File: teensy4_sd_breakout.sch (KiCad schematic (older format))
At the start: 3 parts, among them J1 Conn_01x09, J2 Micro_SD_Card_Det

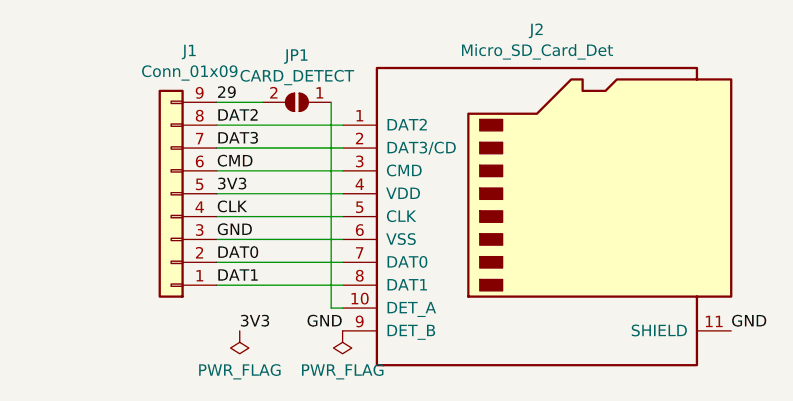
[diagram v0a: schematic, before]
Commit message: Added decoupling cap and back silk screen
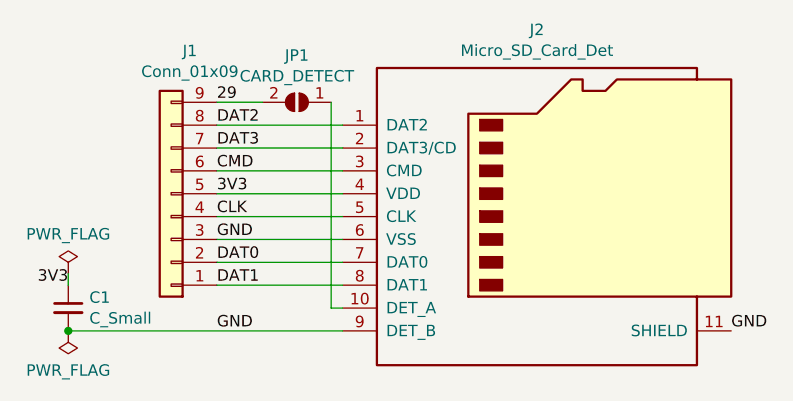
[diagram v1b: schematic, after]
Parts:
- added C1: C_Small, Capacitor_SMD:C_0805_2012Metric_Pad1.15x1.40mm_HandSolder, symbol Device:C_Small
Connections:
- net 3V3: now also C1.1
- net GND: now also C1.2
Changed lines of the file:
@@
 EESchema Schematic File Version 4
+LIBS:teensy4_sd_breakout-cache
 EELAYER 30 0
 EELAYER END
@@
 Text Label 6500 2450 0    50   ~ 0
 DAT2
-$Comp
-L Connector:Micro_SD_Card_Det J2
-U 1 1 5D85967D
-P 7950 2850
-F 0 "J2" H 7900 3667 50  0000 C CNN
-F 1 "Micro_SD_Card_Det" H 7900 3576 50  0000 C CNN
-F 2 "Connector_Card:microSD_HC_Hirose_DM3D-SF" H 10000 3550 50  0001 C CNN
-F 3 "https://www.hirose.com/product/en/download_file/key_name/DM3/category/Catalog/doc_file_id/49662/?file_category_id=4&item_id=195&is_series=1" H 7950 2950 50  0001 C CNN
-	1    7950 2850
-	1    0    0    -1
-$EndComp
 Text Label 8750 3350 0    50   ~ 0
 GND
-Text Label 7050 3350 2    50   ~ 0
+Text Label 6500 3350 0    50   ~ 0
 GND
-Wire Wire Line
-	7050 2450 6500 2450
-Wire Wire Line
-	7050 2550 6500 2550
-Wire Wire Line
-	6500 2650 7050 2650
-Wire Wire Line
-	7050 2750 6500 2750
-Wire Wire Line
-	6500 2850 7050 2850
-Wire Wire Line
-	7050 2950 6500 2950
-Wire Wire Line
-	6500 3050 7050 3050
-Wire Wire Line
-	7050 3150 6500 3150
 $Comp
 L Connector_Generic:Conn_01x09 J1
@@
 Wire Wire Line
 	7000 2350 7000 3250
-Wire Wire Line
-	7000 3250 7050 3250
 Text Label 6500 2350 0    50   ~ 0
 29
 $Comp
+L power:PWR_FLAG #FLG0102
+U 1 1 5D867552
+P 5850 3100
+F 0 "#FLG0102" H 5850 3175 50  0001 C CNN
+F 1 "PWR_FLAG" H 5850 3273 50  0000 C CNN
+F 2 "" H 5850 3100 50  0001 C CNN
+F 3 "~" H 5850 3100 50  0001 C CNN
+	1    5850 3100
+	1    0    0    -1
+$EndComp
+$Comp
+L Device:C_Small C1
+U 1 1 5D8A3C4C
+P 5850 3250
+F 0 "C1" H 5942 3296 50  0000 L CNN
+F 1 "C_Small" H 5942 3205 50  0000 L CNN
+F 2 "Capacitor_SMD:C_0805_2012Metric_Pad1.15x1.40mm_HandSolder" H 5850 3250 50  0001 C CNN
+F 3 "~" H 5850 3250 50  0001 C CNN
+	1    5850 3250
+	1    0    0    -1
+$EndComp
+Text Label 5850 3150 2    50   ~ 0
+3V3
+Wire Wire Line
+	7050 3150 6500 3150
+Wire Wire Line
+	6500 3050 7050 3050
+Wire Wire Line
+	7050 2950 6500 2950
+Wire Wire Line
+	6500 2850 7050 2850
+Wire Wire Line
+	7050 2750 6500 2750
+Wire Wire Line
+	6500 2650 7050 2650
+Wire Wire Line
+	7050 2550 6500 2550
+Wire Wire Line
+	7000 3250 7050 3250
+Wire Wire Line
+	7050 2450 6500 2450
+$Comp
+L Connector:Micro_SD_Card_Det J2
+U 1 1 5D85967D
+P 7950 2850
+F 0 "J2" H 7900 3667 50  0000 C CNN
+F 1 "Micro_SD_Card_Det" H 7900 3576 50  0000 C CNN
+F 2 "Connector_Card:microSD_HC_Hirose_DM3D-SF" H 10000 3550 50  0001 C CNN
+F 3 "https://www.hirose.com/product/en/download_file/key_name/DM3/category/Catalog/doc_file_id/49662/?file_category_id=4&item_id=195&is_series=1" H 7950 2950 50  0001 C CNN
+	1    7950 2850
+	1    0    0    -1
+$EndComp
+$Comp
 L power:PWR_FLAG #FLG0101
 U 1 1 5D86631A
-P 7050 3350
-F 0 "#FLG0101" H 7050 3425 50  0001 C CNN
-F 1 "PWR_FLAG" H 7050 3523 50  0000 C CNN
-F 2 "" H 7050 3350 50  0001 C CNN
-F 3 "~" H 7050 3350 50  0001 C CNN
-	1    7050 3350
+P 5850 3350
+F 0 "#FLG0101" H 5850 3425 50  0001 C CNN
+F 1 "PWR_FLAG" H 5850 3523 50  0000 C CNN
+F 2 "" H 5850 3350 50  0001 C CNN
+F 3 "~" H 5850 3350 50  0001 C CNN
+	1    5850 3350
 	-1   0    0    1
 $EndComp
-$Comp
-L power:PWR_FLAG #FLG0102
-U 1 1 5D867552
-P 6600 3350
-F 0 "#FLG0102" H 6600 3425 50  0001 C CNN
-F 1 "PWR_FLAG" H 6600 3523 50  0000 C CNN
-F 2 "" H 6600 3350 50  0001 C CNN
-F 3 "~" H 6600 3350 50  0001 C CNN
-	1    6600 3350
-	-1   0    0    1
-$EndComp
-Text Label 6600 3350 0    50   ~ 0
-3V3
+Connection ~ 5850 3350
+Wire Wire Line
+	5850 3350 7050 3350
+Wire Wire Line
+	5850 3100 5850 3150
 $EndSCHEMATC

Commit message: Updated documentation and silkscreen
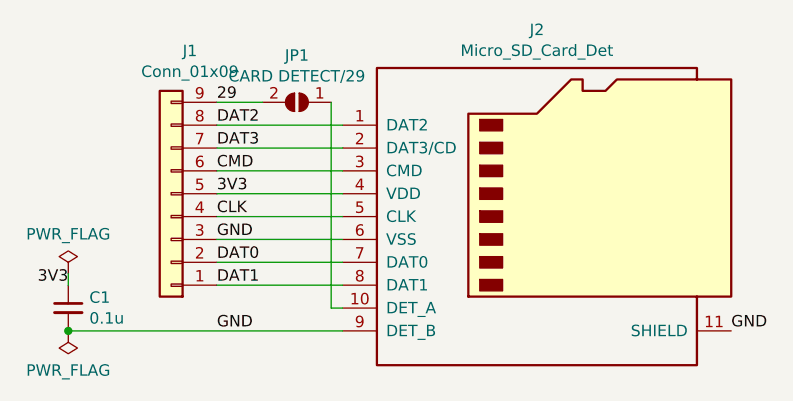
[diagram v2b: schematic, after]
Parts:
- C1: value C_Small -> 0.1u
- JP1: value CARD_DETECT -> CARD DETECT/29
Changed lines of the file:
@@
 P 6850 2350
 F 0 "JP1" H 6850 2555 50  0000 C CNN
-F 1 "CARD_DETECT" H 6850 2464 50  0000 C CNN
+F 1 "CARD DETECT/29" H 6850 2464 50  0000 C CNN
 F 2 "Jumper:SolderJumper-2_P1.3mm_Open_RoundedPad1.0x1.5mm" H 6850 2350 50  0001 C CNN
 F 3 "~" H 6850 2350 50  0001 C CNN
@@
 P 5850 3250
 F 0 "C1" H 5942 3296 50  0000 L CNN
-F 1 "C_Small" H 5942 3205 50  0000 L CNN
+F 1 "0.1u" H 5942 3205 50  0000 L CNN
 F 2 "Capacitor_SMD:C_0805_2012Metric_Pad1.15x1.40mm_HandSolder" H 5850 3250 50  0001 C CNN
 F 3 "~" H 5850 3250 50  0001 C CNN
